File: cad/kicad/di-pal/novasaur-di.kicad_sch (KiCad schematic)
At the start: 41 parts, among them J1 GAL16V4, U1 1G19, U10 1G19, U11 1G11, U12 1G374, U13 1G374, U14 1G19, U15 1G19, U16 1G19, U17 1G11, U18 1G374, U19 1G19, U2 1G19, U20 1G86, U21 1G11, U22 1G86, U23 1G374, U24 1G86, U25 1G19, U26 1G19, U27 1G19, U28 1G19, U29 1G19, U3 1G19, U30 1G19, U31 1G19, U32 1G19, U33 1G11, U34 1G19, U35 1G11, U36 1G19, U37 1G11, U38 1G19, U39 1G11, U4 1G19, U40 1G19, U5 1G19, U6 1G19, U7 1G11, U8 1G11, U9 1G19

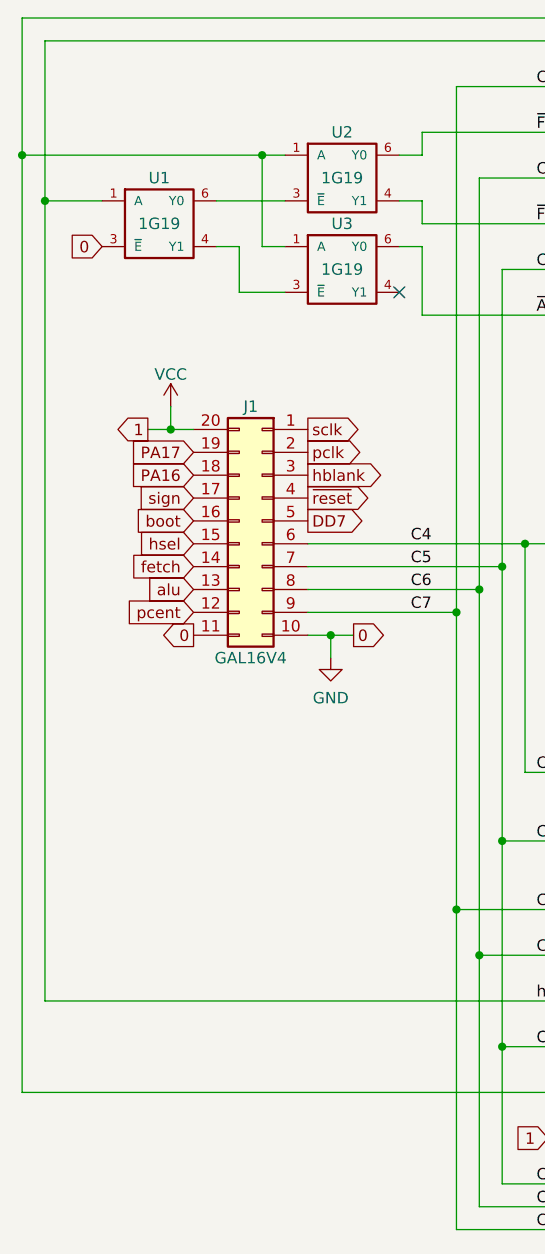
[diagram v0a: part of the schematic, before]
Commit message: fix fetch/hsel mixup
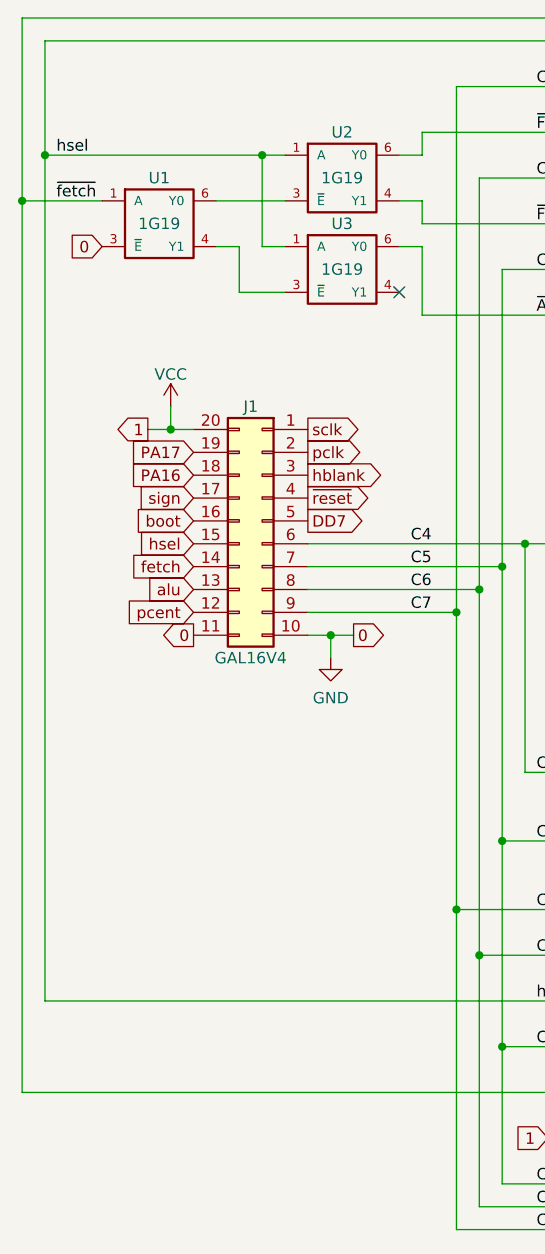
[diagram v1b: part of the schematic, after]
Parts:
- U1, U10, U11, U12, U13, U14, U15, U16, U17, U18, U19, U2, U21, U23, U25, U26, U27, U28, U29, U3, U30, U31, U32, U33, U34, U35, U36, U37, U38, U39, U4, U40, U5, U6, U7, U8, U9: footprint Package_TO_SOT_SMD:SOT-23-6_Handsoldering -> Package_TO_SOT_SMD:SOT-363_SC-70-6
- U20, U22, U24: footprint Package_TO_SOT_SMD:SOT-23-6_Handsoldering -> Package_TO_SOT_SMD:SOT-353_SC-70-5
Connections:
- net hsel: now also U2.1 (A), U3.1 (A); no longer U1.1 (A)
- net ~{fetch}: now also U1.1 (A); no longer U2.1 (A), U3.1 (A)

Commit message: fix moar fetch/hsel mixup
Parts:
- removed U14: 1G19, Package_TO_SOT_SMD:SOT-363_SC-70-6, symbol 74xGxx:74AUC1G19
- added U9: 1G19, Package_TO_SOT_SMD:SOT-363_SC-70-6, symbol 74xGxx:74AUC1G19
- renumbered U9 to U10, U10 to U11, U11 to U12, U12 to U13, U13 to U14, U20 to U19, U21 to U20, U22 to U21, U23 to U22, U24 to U23, U25 to U24, U26 to U25, U27 to U26, U28 to U27, U29 to U28, U30 to U29, U31 to U30, U32 to U31, U33 to U32, U34 to U33, U35 to U34, U36 to U35, U37 to U36, U38 to U37, U39 to U38, U40 to U39, U19 to U40
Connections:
- net C6: now also U4.1 (A); no longer U5.1 (A)
- net C7: now also U5.1 (A); no longer U4.1 (A)
- net GND: now also U9.2 (GND)
- net VCC: now also U7.6, U9.5 (VCC)
- net fetch: now also U1.4 (Y1), U3.3 (~{E})
- net ~{AL}: now also U3.4 (Y1); no longer U3.6 (Y0)
- net ~{FH}: now also U2.6 (Y0), U4.3 (~{E}); no longer U2.4 (Y1), U5.3 (~{E})
- net ~{FL}: now also U2.4 (Y1), U5.3 (~{E}); no longer U2.6 (Y0), U4.3 (~{E})
- net ~{reset}: now also U9.1 (A); no longer U7.6
- net at U7.4: now also U9.3 (~{E}); no longer U13.3 (D)
- new net: U13.3 (D), U9.4 (Y1)
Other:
- moved on the sheet: U1, U2, U3
